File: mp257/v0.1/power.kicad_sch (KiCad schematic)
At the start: 138 parts, among them U26 STPMIC25APQR, U4 STM32MP257FAK3, U9 MCP1501-18xCH

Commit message: Fix ref nums pasted from reference schematic
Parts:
- removed B2: SW_PUSH_SMD_2P, SWI_WE_434121025816, symbol MCD_PARTS_database:U_PMIC_0_SW_PUSH_SMD_2P_MCD_PARTS_database.DbLib
- removed C10, C15, C18, C20, C22 (x2), C23, C26 (x2), C27, C28 (x2), C30, C35 (x2), C36, C8, C9: Capacitor, C0603, symbol MCD_PARTS_database:U_PMIC_1_Capacitor_MCD_PARTS_database.DbLib
- removed C11, C7: Capacitor, C0402, symbol MCD_PARTS_database:U_PMIC_1_Capacitor_MCD_PARTS_database.DbLib
- removed C155, C16, C34, C38: Capacitor, C0402, symbol MCD_PARTS_database:U_PMIC_0_Capacitor_MCD_PARTS_database.DbLib
- removed C17, C37, C39: Capacitor, C0402, symbol MCD_PARTS_database:U_PMIC_2_Capacitor_MCD_PARTS_database.DbLib
- removed C19 (x2), C20, C23, C25, C27, C30, C36: Capacitor, C0805, symbol MCD_PARTS_database:U_PMIC_1_Capacitor_MCD_PARTS_database.DbLib
- removed C50, C51, C71, C82, C85, C96, C97: Capacitor, C0201_MURATA_GRM033_H0P3, symbol MCD_PARTS_database:U_STM32MP25XXAK Power_1_Capacitor_MCD_PARTS_database.DbLib
- removed C50, C51, C52 (x2), C55, C57, C58 (x2), C59 (x2), C60, C61, C62, C64 (x2), C71, C73, C74 (x2), C77, C78, C79, C80, C82, C87, C93, C95: ${ALTIUM_VALUE}, C0201_MURATA_GRM033_H0P3, symbol MCD_PARTS_database:U_STM32MP25XXAK Power_1_Capacitor_MCD_PARTS_database.DbLib
- removed C53, C54, C65, C66, C70 (x2): ${ALTIUM_VALUE}, C0201_MURATA_GRM033_H0P3, symbol MCD_PARTS_database:U_STM32MP25XXAK Power_3_Capacitor_MCD_PARTS_database.DbLib
- removed C87: ~, C0402, symbol MCD_PARTS_database:U_STM32MP25XXAK Power_1_Capacitor_MCD_PARTS_database.DbLib
- removed L5 (x2), L6, L7 (x2): Inductor, IND_2016_MURATA_LQM2MPN2R2NG0, symbol MCD_PARTS_database:U_PMIC_0_Inductor_MCD_PARTS_database.DbLib
- removed L6, L8: Inductor, IND_2520_TOKO_DFE252012P, symbol MCD_PARTS_database:U_PMIC_0_Inductor_MCD_PARTS_database.DbLib
- removed R12, R13, R14, R9: ~, R0402, symbol MCD_PARTS_database:U_PMIC_0_Resistor_MCD_PARTS_database.DbLib
- removed R15: Resistor, R0603, symbol MCD_PARTS_database:U_STM32MP25XXAK Power_0_Resistor_MCD_PARTS_database.DbLib
- removed R17: Resistor, R0402, symbol MCD_PARTS_database:U_STM32MP25XXAK Power_2_Resistor_MCD_PARTS_database.DbLib
- removed U4: STM32MP257FAK3, ICC_TFBGA424_14X14_P050_H1P20_CODE-B0A2, symbol MCD_PARTS_database:U_STM32MP25XXAK Power_0_STM32MP257FAK3_MCD_PARTS_database.Db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
- added C1, C10, C11, C13, C2, C3, C4, C45, C46, C48, C49, C5, C50, C51, C52, C58, C59, C64, C68, C69, C7, C71, C72, C74, C75, C76, C82: ${ALTIUM_VALUE}, C0201_MURATA_GRM033_H0P3, symbol MCD_PARTS_database:U_STM32MP25XXAK Power_1_Capacitor_MCD_PARTS_database.DbLib
- added C12, C44, C47, C6, C70, C8: ${ALTIUM_VALUE}, C0201_MURATA_GRM033_H0P3, symbol MCD_PARTS_database:U_STM32MP25XXAK Power_3_Capacitor_MCD_PARTS_database.DbLib
- added C15, C16, C17, C192, C195, C196, C201: Capacitor, C0201_MURATA_GRM033_H0P3, symbol MCD_PARTS_database:U_STM32MP25XXAK Power_1_Capacitor_MCD_PARTS_database.DbLib
- added C183, C184, C199, C20, C200, C202, C22, C23, C24, C26, C27, C28, C29, C30, C32, C35, C36, C41: Capacitor, C0603, symbol MCD_PARTS_database:U_PMIC_1_Capacitor_MCD_PARTS_database.DbLib
- added C186, C187, C19, C193, C204, C206, C207, C21: Capacitor, C0805, symbol MCD_PARTS_database:U_PMIC_1_Capacitor_MCD_PARTS_database.DbLib
- added C188, C209: Capacitor, C0402, symbol MCD_PARTS_database:U_PMIC_1_Capacitor_MCD_PARTS_database.DbLib
- added C189, C40, C43: Capacitor, C0402, symbol MCD_PARTS_database:U_PMIC_2_Capacitor_MCD_PARTS_database.DbLib
- added C190, C208, C91: Capacitor, C0402, symbol MCD_PARTS_database:U_PMIC_0_Capacitor_MCD_PARTS_database.DbLib
- added C87: ~, C0402, symbol MCD_PARTS_database:U_STM32MP25XXAK Power_1_Capacitor_MCD_PARTS_database.DbLib
- added L1, L3, L5, L6, L7: Inductor, IND_2016_MURATA_LQM2MPN2R2NG0, symbol MCD_PARTS_database:U_PMIC_0_Inductor_MCD_PARTS_database.DbLib
- added L2, L4: Inductor, IND_2520_TOKO_DFE252012P, symbol MCD_PARTS_database:U_PMIC_0_Inductor_MCD_PARTS_database.DbLib
- added R11: Resistor, R0603, symbol MCD_PARTS_database:U_STM32MP25XXAK Power_0_Resistor_MCD_PARTS_database.DbLib
- added R2, R59, R60, R81: ~, R0402, symbol MCD_PARTS_database:U_PMIC_0_Resistor_MCD_PARTS_database.DbLib
- added R269: ~, R0402, symbol MCD_PARTS_database:U_STM32MP25XXAK Power_0_Resistor_MCD_PARTS_database.DbLib
- added R67: Resistor, R0402, symbol MCD_PARTS_database:U_STM32MP25XXAK Power_2_Resistor_MCD_PARTS_database.DbLib
- added U1: STM32MP257FAK3, ICC_TFBGA424_14X14_P050_H1P20_CODE-B0A2, symbol MCD_PARTS_database:U_STM32MP25XXAK Power_0_STM32MP257FAK3_MCD_PARTS_database.Db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
- renumbered C5 to C33
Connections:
- net +3V3: now also C204.2, C206.2, C207.2, C21.2, L7.2
- net +5V: now also C184.2, C188.2, C199.2, C20.2, C209.2, C29.2, C30.2, C32.2
- net 1V8: now also C193.2, L1.2, R269.1, U1.1E1 (VDDA18PLL3), U1.AD22 (VDDA18USB), U1.AE23 (VDDA18COMBOPHY), U1.D18 (VDDIO2), U1.E17 (VDDIO2), U1.F20 (VDDA18DDR), U1.G19 (VDDA18PLL1), U1.G5 (VDDA18LVDS), U1.G7 (VDDA18CSI), U1.G9 (VDDA18DSI), U1.H6 (VDDA18PLL2); no longer C248.2, C250.2
- net GND: now also C1.1, C10.1, C11.1, C12.2, C13.1, C15.1, C16.1, C17.1, C183.1, C184.1, C186.1, C187.1, C188.1, C189.1, C19.1, C190.2, C192.1, C193.1, C195.1, C196.1, C199.1, C2.1, C20.1, C200.1, C201.1, C202.1, C204.1, C206.1, C207.1, C208.2, C209.1, C21.1, C22.1, C23.1, C24.1, C26.1, C27.1, C28.1, C29.1, C3.1, C30.1, C32.1, C35.1, C36.1, C4.1, C40.1, C41.1, C43.1, C44.2, C45.1, C46.1, C47.2, C48.1, C49.1, C5.1, C50.1, C51.1, C52.1, C58.1, C59.1, C6.2, C64.1, C68.1, C69.1, C7.1, C70.2, C71.1, C72.1, C74.1, C75.1, C76.1, C8.2, C82.1, C87.1, C91.2, U1.1A1 (VSS), U1.1A11 (VSS), U1.1A3 (VSS), U1.1A5 (VSS), U1.1A7 (VSS), U1.1A9 (VSS), U1.1B10 (VSS), U1.1B12 (VSS), U1.1B2 (VSS), U1.1B4 (VSS), U1.1B6 (VSS), U1.1B8 (VSS), U1.1E7 (VSS), U1.1E9 (VSS), U1.1F10 (VSS), U1.1F6 (VSS), U1.1F8 (VSS), U1.1G1 (VSS), U1.1G11 (VSS), U1.1G3 (VSS), U1.1G5 (VSS), U1.1H12 (VSS), U1.1H2 (VSS), U1.1H4 (VSS), U1.1J1 (VSS), U1.1J11 (VSS), U1.1J3 (VSS), U1.1J5 (VSS), U1.1J7 (VSS), U1.1J9 (VSS), U1.1K10 (VSS), U1.1K12 (VSS), U1.1K2 (VSS), U1.1K4 (VSS), U1.1K6 (VSS), U1.1K8 (VSS), U1.A1 (VSS), U1.A2 (VSS), U1.A27 (VSS), U1.AC11 (VSS), U1.AC3 (VSSAON), U1.AC5 (VSSA), U1.AF6 (VREFN), U1.AG1 (VSS), U1.AG27 (VSS), U1.C10 (VSS), U1.C6 (VSS), U1.E7 (VSS), U1.F12 (VSS), U1.F14 (VSS), U1.F16 (VSS), U1.F3 (VSS), U1.J7 (VSS), U1.K3 (VSS), U1.V6 (VSS), U1.Y4 (VSS)
- net NRST: now also R81.1
- net NRSTC1MS: now also R59.1
- net PWR_CPU_ON: now also R60.1
- net PWR_ON: now also R2.1
- net VDDA1V8_AON: now also C189.2, U1.AB3 (VDDA18AON)
- net VDDCORE: now also C16.2, C183.2, C192.2, C201.2, C22.2, C23.2, C24.2, C44.1, C45.2, C46.2, C47.1, C48.2, C49.2, C50.2, C51.2, L2.2, R11.1, U1.1C1 (VDDCORE), U1.1C3 (VDDCORE), U1.1C5 (VDDCORE), U1.1D2 (VDDCORE), U1.1D4 (VDDCORE), U1.1E3 (VDDCORE), U1.1E5 (VDDCORE), U1.1F2 (VDDCORE), U1.1F4 (VDDCORE), U1.E5 (VDDCSI), U1.F4 (VDDLVDS), U1.F8 (VDDDSI)
- net VDDCPU: now also C10.2, C11.2, C26.2, C27.2, C28.2, C6.1, C64.2, C68.2, C69.2, C7.2, C8.1, L3.2, U1.1C7 (VDDCPU), U1.1C9 (VDDCPU), U1.1D10 (VDDCPU), U1.1D6 (VDDCPU), U1.1D8 (VDDCPU), U1.F18 (VDDCPU), U1.G15 (VDDCPU), U1.G17 (VDDCPU)
- net VDDGPU: now also C1.2, C2.2, C3.2, C35.2, C36.2, C4.2, C5.2, C52.2, C58.2, C59.2, L4.2, U1.1G7 (VDDGPU), U1.1G9 (VDDGPU), U1.1H10 (VDDGPU), U1.1H6 (VDDGPU), U1.1H8 (VDDGPU), U1.1L7 (VDDGPU), U1.1L9 (VDDGPU), U1.1M10 (VDDGPU), U1.1M6 (VDDGPU), U1.1M8 (VDDGPU)
- net VDDIO: now also C12.1, C17.2, C186.2, C187.2, C19.2, C196.2, C70.1, C71.2, C72.2, C74.2, L6.2, R67.2, U1.1L1 (VDD), U1.1L3 (VDD), U1.1L5 (VDD), U1.1M2 (VDD), U1.1M4 (VDD), U1.D10 (VDDIO3), U1.E11 (VDDIO3), U1.E9 (VDDIO4), U1.G11 (VDDIO4)
- net VDDIO_SDCARD: now also C195.2, U1.D14 (VDDIO1), U1.E13 (VDDIO1)
- net VDD_DDR: now also C13.2, C200.2, C202.2, C41.2, C75.2, C76.2, C82.2, L5.2, U1.1C11 (VDDQDDR), U1.1D12 (VDDQDDR), U1.1E11 (VDDQDDR), U1.1F12 (VDDQDDR), U1.1L11 (VDDQDDR), U1.1M12 (VDDQDDR), U1.M22 (VDDQDDR), U1.N21 (VDDQDDR), U1.R21 (VDDQDDR)
- net VDD_EMMC: now also C190.1
- net VPP_DDR: now also C91.1
- net VREF+: now also C248.2, C250.2, R269.2, U1.AG6 (VREFP)
- net VTT_DDR: now also C40.2
- net at C251.2, R286.2: now also U1.AE21 (VDD33USB), U1.AE22 (VDD33UCPD)
- net at U26.37 (VLX5): now also L1.1
- net at U26.55 (PWRCTRL2): now also R60.2
- net at U26.56 (PWRCTRL1): now also R2.2
- net at C252.2, C260.2: now also C15.2, R11.2, U1.AB20 (VDDCOMBOPHY), U1.AB22 (VDDCOMBOPHYTX), U1.AC21 (VDDPCIECLK)
- net at U26.51 (VLX7): now also L7.1
- net WAKEUP_BUT: now reaches U26.1 (PONKEYn)
- net at U26.19 (VLX4): now also L6.1
- net at U26.23 (VLX3): now also L4.1
- net at U26.26 (VLX2): now also L2.1
- net at U26.31 (RSTn): now also R81.2
- net at U26.40 (VLX1): now also L3.1
- net at U26.45 (REFDDR): now also C43.2
- net at U26.48 (VLX6): now also L5.1
- net at U26.54 (PWRCTRL3): now also R59.2
- net at U26.8 (INTLDO): now also C208.1
- net at C235.2, C244.2, R267.1: now also U1.AB6 (VDDA18ADC)
- net at C225.2: now also U1.R7 (V08CAP)
- new net VBAT: C87.2, R67.1, U1.T6 (VBAT)
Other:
- note removed: "WAKE UP"
- moved on the sheet: C41, C44, U9

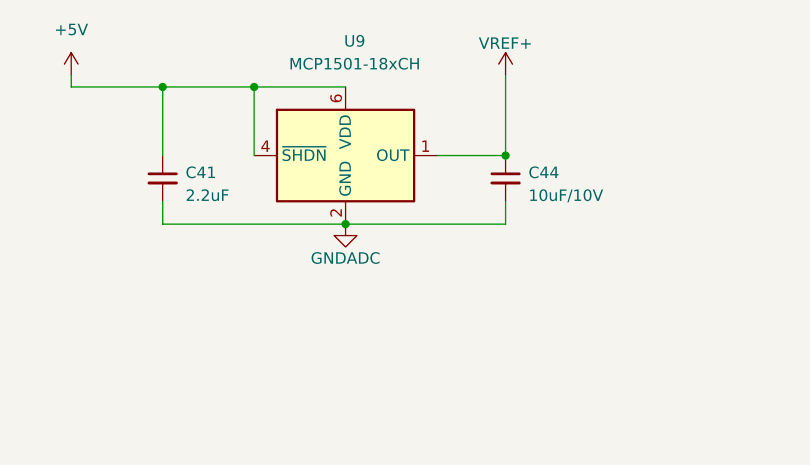
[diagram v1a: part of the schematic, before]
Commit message: Fix all refs: no duplicates
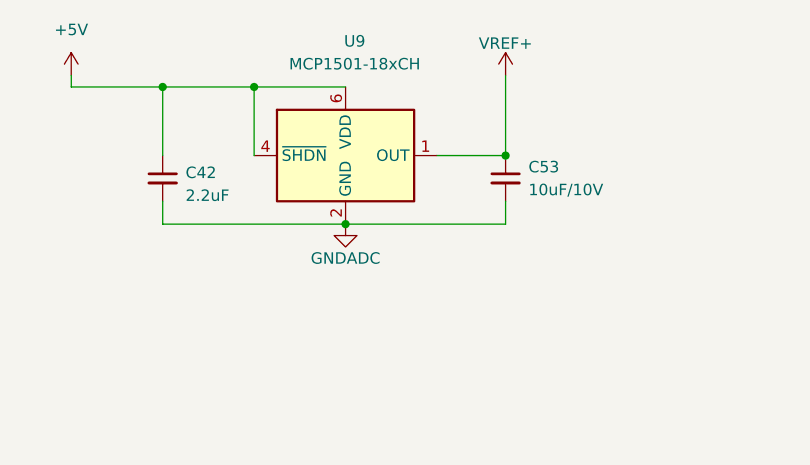
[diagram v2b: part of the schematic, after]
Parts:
- renumbered C41 to C42, C44 to C53

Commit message: WIP: symbols
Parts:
- removed C250: Capacitor, C0201_MURATA_GRM033_H0P3, symbol MCD_PARTS_database:U_STM32MP25XXAK Power_1_Capacitor_MCD_PARTS_database.DbLib
- removed R269: ~, R0402, symbol MCD_PARTS_database:U_STM32MP25XXAK Power_0_Resistor_MCD_PARTS_database.DbLib
- removed R67: Resistor, R0402, symbol MCD_PARTS_database:U_STM32MP25XXAK Power_2_Resistor_MCD_PARTS_database.DbLib
- added NT1: NetTie, 4ms_SolderJumper:NetTie-2_SMD_Pad0.16mm_6mil, symbol 4ms_Net_Tie:NetTie
- U1: symbol MCD_PARTS_database:U_STM32MP25XXAK Power_0_STM32MP257FAK3_MCD_PARTS_database.DbLib -> 4ms_IC:STM32MP257FAKx
- U26: footprint ICC_QFN56-EPAD_6P5X6P5_P040 -> 4ms_Package_QFP:QFN-56_EP_7x7_Pitch0.4mm; symbol MCD_PARTS_database:U_PMIC_0_STPMIC2_MCD_PARTS_database.DbLib -> 4ms_IC:STPMIC25APQR; ALTIUM_VALUE STPMIC25APQR -> (none); COMPONENTLINK1DESCRIPTION Datasheet -> (none); COMPONENTLINK1URL http://tunmcdsvn.tun.st.com/Component_Documentation_Library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 -> (none); COMPONENT_COUNTRY_OF_ORIGIN Unknown -> (none); ID 5116 -> (none); INTERNAL_PART_NUMBER MCD-03000 -> (none); MANUFACTURER STMICROELECTRONICS -> (none); MANUFACTURER_PART_NUMBER STPMIC25APQR -> (none); Manufacturer (none) -> STMICROELECTRONICS; ORDER_CODE_DIGIKEY N/A -> (none); ORDER_CODE_FARNELL N/A -> (none); ORDER_CODE_RS N/A -> (none); PACKAGE VQFN -> (none); PART_PREFERENCE Recommended -> (none); PART_TYPE IC -> (none); Part Number (none) -> STPMIC25APQR; SHOWFIELDS YES -> (none); STATUS Released -> (none)
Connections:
- net VDDIO is gone; now on net VDD_IO: C12.1, C17.2, C186.2, C187.2, C19.2, C196.2, C70.1, C71.2, C72.2, C74.2, L6.2, LNK11.2, R260.2, R261.2, U1.1L1 (VDD), U1.1L3 (VDD), U1.1L5 (VDD), U1.1M2 (VDD), U1.1M4 (VDD), U1.D10 (VDDIO3), U1.E11 (VDDIO3), U1.E9 (VDDIO4), U1.G11 (VDDIO4), U26.29 (VIO)
- net GND: now also NT1.1; no longer U1.AF6 (VREFN)
- net GNDADC: now also U1.AF6 (VREFN), NT1.2
- net 1V8 renamed +1V8
- net 5V_VCONN: no longer names the net of C1141.1, U26.5 (LDO6OUT)
- net VBAT renamed VDD_IO
- net VDD3V3_USB renamed VDD_USB
- net VDDA1V8_AON renamed VDDA_1V8
- net VDDCORE renamed VDD_CORE
- net VDDCPU renamed VDD_CPU
- net VDDGPU renamed VDD_GPU
- net VDD_EMMC: no longer names the net of C190.1, U26.16 (LDO2OUT)
- net VDD_SDCARD: no longer names the net of C142.1, U26.4 (LDO7OUT)
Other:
- note added: "5V_VCONN"
- note added: "Not used"
- note added: "VDD_EMMC"
- note added: "VDD_SDCARD"
- moved on the sheet: C1141, C142, C16, C217, C91

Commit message: Updated RAM and STM32MP2 footprints to 4ms lib
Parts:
- U1: footprint ICC_TFBGA424_14X14_P050_H1P20_CODE-B0A2 -> 4ms_Package_QFP:TFBGA-424_14x14mm_P0.5_STM_AK

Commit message: Updating parts to 4ms lib
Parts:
- C1, C10, C11, C13, C2, C3, C4, C45, C46, C48, C49, C5, C50, C51, C52, C58, C59, C64, C68, C69, C7, C71, C72, C74, C75, C76, C82: value ${ALTIUM_VALUE} -> 1uF_0201_4V; footprint C0201_MURATA_GRM033_H0P3 -> 4ms_Capacitor:C_0201; symbol MCD_PARTS_database:U_STM32MP25XXAK Power_1_Capacitor_MCD_PARTS_database.DbLib -> 4ms_Capacitor:1uF_0201_4V; ALTIUM_VALUE 1uF -> (none); COMPONENTLINK1URL http://tunmcdsvn.tun.st.com/Component_Documentation_Library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 -> (none); COMPONENT_COUNTRY_OF_ORIGIN Japan -> (none); Display (none) -> 1uF; ID 4483 -> (none); INTERNAL_PART_NUMBER MCD-02377 -> (none); JLCPCB ID (none) -> C272877; MANUFACTURER MURATA -> (none); MANUFACTURER_PART_NUMBER GRM033R60J105MEA2 -> (none); Manufacturer (none) -> Yageo; Manufacturer 2 (none) -> Murata; ORDER_CODE_DIGIKEY 490-7229-2-ND -> (none); ORDER_CODE_FARNELL 2470448 -> (none); ORDER_CODE_RS 820-0643 -> (none); PACKAGE 0201 -> (none); PART_PREFERENCE Recommended -> (none); PART_TYPE Capacitor -> (none); Part Number (none) -> CC0201MRX5R5BB105; Part Number 2 (none) -> GRM033D70G105ME01D; Production Stage (none) -> A; SHOWFIELDS YES -> (none); STATUS Checked -> (none); Specifications (none) -> 1uF, Min. 4V 10%, X7R or X5R or X6S or similar
- C1141, C142, C190, C208, C217, C91: value Capacitor -> 4.7uF_0402_6.3V; footprint C0402 -> 4ms_Capacitor:C_0402; symbol MCD_PARTS_database:U_PMIC_0_Capacitor_MCD_PARTS_database.DbLib -> 4ms_Capacitor:4.7uF_0402_6.3V; ALTIUM_VALUE 4.7uF -> (none); COMPONENTLINK1URL http://tunmcdsvn.tun.st.com/Component_Documentation_Library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 -> (none); COMPONENT_COUNTRY_OF_ORIGIN Japan -> (none); Display (none) -> 4.7uF; ID 3456 -> (none); INTERNAL_PART_NUMBER MCD-01356 -> (none); JLCPCB ID (none) -> C23733; MANUFACTURER MURATA -> (none); MANUFACTURER_PART_NUMBER GRM155R60J475ME47 -> (none); Manufacturer (none) -> Murata; ORDER_CODE_DIGIKEY 490-5915-1-ND -> (none); ORDER_CODE_FARNELL 2666407 -> (none); ORDER_CODE_RS 814-5230 -> (none); PACKAGE 0402 -> (none); PART_PREFERENCE Recommended -> (none); PART_TYPE Capacitor -> (none); Part Number (none) -> GRM155R60J475ME47; Production Stage (none) -> A; SHOWFIELDS YES -> (none); STATUS Released -> (none); Specifications (none) -> 4.7uF, Min. 6.3V 20%, X7R or X5R or similar
- C12, C44, C47, C6, C70, C77, C8: value ${ALTIUM_VALUE} -> 1uF_0201_4V; footprint C0201_MURATA_GRM033_H0P3 -> 4ms_Capacitor:C_0201; symbol MCD_PARTS_database:U_STM32MP25XXAK Power_3_Capacitor_MCD_PARTS_database.DbLib -> 4ms_Capacitor:1uF_0201_4V; ALTIUM_VALUE 1uF -> (none); COMPONENTLINK1URL http://tunmcdsvn.tun.st.com/Component_Documentation_Library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 -> (none); COMPONENT_COUNTRY_OF_ORIGIN Japan -> (none); Display (none) -> 1uF; ID 4483 -> (none); INTERNAL_PART_NUMBER MCD-02377 -> (none); JLCPCB ID (none) -> C272877; MANUFACTURER MURATA -> (none); MANUFACTURER_PART_NUMBER GRM033R60J105MEA2 -> (none); Manufacturer (none) -> Yageo; Manufacturer 2 (none) -> Murata; ORDER_CODE_DIGIKEY 490-7229-2-ND -> (none); ORDER_CODE_FARNELL 2470448 -> (none); ORDER_CODE_RS 820-0643 -> (none); PACKAGE 0201 -> (none); PART_PREFERENCE Recommended -> (none); PART_TYPE Capacitor -> (none); Part Number (none) -> CC0201MRX5R5BB105; Part Number 2 (none) -> GRM033D70G105ME01D; Production Stage (none) -> A; SHOWFIELDS YES -> (none); STATUS Checked -> (none); Specifications (none) -> 1uF, Min. 4V 10%, X7R or X5R or X6S or similar
- C15, C252, C260: value Capacitor -> 1uF_0201_4V; footprint C0201_MURATA_GRM033_H0P3 -> 4ms_Capacitor:C_0201; symbol MCD_PARTS_database:U_STM32MP25XXAK Power_1_Capacitor_MCD_PARTS_database.DbLib -> 4ms_Capacitor:1uF_0201_4V; ALTERNATE_MANUFACTURER N/A -> (none); ALTERNATE_MANUFACTURER_PART_NUMBER N/A -> (none); ALTIUM_VALUE 1uF -> (none); COMPONENTLINK1URL http://tunmcdsvn.tun.st.com/Component_Documentation_Library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 -> (none); COMPONENT_COUNTRY_OF_ORIGIN Japan -> (none); Display (none) -> 1uF; ID 4483 -> (none); INTERNAL_PART_NUMBER MCD-02377 -> (none); JLCPCB ID (none) -> C272877; MANUFACTURER MURATA -> (none); MANUFACTURER_PART_NUMBER GRM033R60J105MEA2 -> (none); Manufacturer (none) -> Yageo; Manufacturer 2 (none) -> Murata; ORDER_CODE_DIGIKEY 490-7229-2-ND -> (none); ORDER_CODE_FARNELL 2470448 -> (none); ORDER_CODE_RS 820-0643 -> (none); PACKAGE 0201 -> (none); PART_PREFERENCE Recommended -> (none); PART_TYPE Capacitor -> (none); Part Number (none) -> CC0201MRX5R5BB105; Part Number 2 (none) -> GRM033D70G105ME01D; Production Stage (none) -> A; SHOWFIELDS YES -> (none); STATUS Checked -> (none); Specifications (none) -> 1uF, Min. 4V 10%, X7R or X5R or X6S or similar
- C152, C157, C186, C187, C19, C193, C204, C206, C207, C21: value Capacitor -> 22uF_0805_10V; footprint C0805 -> 4ms_Capacitor:C_0805; symbol MCD_PARTS_database:U_PMIC_1_Capacitor_MCD_PARTS_database.DbLib -> 4ms_Capacitor:22uF_0805_10V; ALTIUM_VALUE 22uF -> (none); COMPONENTLINK1URL http://tunmcdsvn.tun.st.com/Component_Documentation_Library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 -> (none); COMPONENT_COUNTRY_OF_ORIGIN China, Japan -> (none); Display (none) -> 22uF/10V; ID 5255 -> (none); INTERNAL_PART_NUMBER MCD-03139 -> (none); JLCPCB ID (none) -> C45783; MANUFACTURER MURATA -> (none); MANUFACTURER_PART_NUMBER GRM21BR61A226ME51L -> (none); Manufacturer (none) -> Taiyo Yuden; ORDER_CODE_DIGIKEY 490-10511-2-ND -> (none); ORDER_CODE_FARNELL 2494270 -> (none); ORDER_CODE_RS N/A -> (none); PACKAGE 0805 -> (none); PART_PREFERENCE Recommended -> (none); PART_TYPE Capacitor -> (none); Part Number (none) -> LMK212BBJ226MG-T; Production Stage (none) -> A; SHOWFIELDS YES -> (none); STATUS Checked -> (none); Specifications (none) -> 22uF, Min. 10V, 20%, X5R or X7S or similar, 0805, MLCC
- C153, C154, C188: value Capacitor -> 1uF_0402_25V; footprint C0402 -> 4ms_Capacitor:C_0402; symbol MCD_PARTS_database:U_PMIC_1_Capacitor_MCD_PARTS_database.DbLib -> 4ms_Capacitor:1uF_0402_25V; ALTIUM_VALUE 1uF -> (none); COMPONENTLINK1URL http://tunmcdsvn.tun.st.com/Component_Documentation_Library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 -> (none); COMPONENT_COUNTRY_OF_ORIGIN Japan -> (none); Display (none) -> 1uF; ID 2772 -> (none); INTERNAL_PART_NUMBER MCD-00095 -> (none); JLCPCB ID (none) -> C52923; MANUFACTURER MURATA -> (none); MANUFACTURER_PART_NUMBER GRM155R61E105KA12 -> (none); Manufacturer (none) -> Taiyo Yuden; Manufacturer 2 (none) -> Murata; ORDER_CODE_DIGIKEY 490-10017-1-ND -> (none); ORDER_CODE_FARNELL 2218855 -> (none); ORDER_CODE_RS 846-7287 -> (none); PACKAGE 0402 -> (none); PART_PREFERENCE Recommended -> (none); PART_TYPE Capacitor -> (none); Part Number (none) -> GMK105CC6105KV-F; Part Number 2 (none) -> GRM155C81E105ME11J; Production Stage (none) -> A; SHOWFIELDS YES -> (none); STATUS Released -> (none); Specifications (none) -> 1uF, Min. 25V, 0402, Ceramic/MLCC
- C156, C189: value Capacitor -> 4.7uF_0402_6.3V; footprint C0402 -> 4ms_Capacitor:C_0402; symbol MCD_PARTS_database:U_PMIC_2_Capacitor_MCD_PARTS_database.DbLib -> 4ms_Capacitor:4.7uF_0402_6.3V; ALTIUM_VALUE 4.7uF -> (none); COMPONENTLINK1URL http://tunmcdsvn.tun.st.com/Component_Documentation_Library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 -> (none); COMPONENT_COUNTRY_OF_ORIGIN Japan -> (none); Display (none) -> 4.7uF; ID 3456 -> (none); INTERNAL_PART_NUMBER MCD-01356 -> (none); JLCPCB ID (none) -> C23733; MANUFACTURER MURATA -> (none); MANUFACTURER_PART_NUMBER GRM155R60J475ME47 -> (none); Manufacturer (none) -> Murata; ORDER_CODE_DIGIKEY 490-5915-1-ND -> (none); ORDER_CODE_FARNELL 2666407 -> (none); ORDER_CODE_RS 814-5230 -> (none); PACKAGE 0402 -> (none); PART_PREFERENCE Recommended -> (none); PART_TYPE Capacitor -> (none); Part Number (none) -> GRM155R60J475ME47; Production Stage (none) -> A; SHOWFIELDS YES -> (none); STATUS Released -> (none); Specifications (none) -> 4.7uF, Min. 6.3V 20%, X7R or X5R or similar
- C16, C17, C192, C195, C196, C201, C220, C234, C236, C237, C238, C239, C240, C244, C246, C248, C251, C253: value Capacitor -> 100nF_0201_16V; footprint C0201_MURATA_GRM033_H0P3 -> 4ms_Capacitor:C_0201; symbol MCD_PARTS_database:U_STM32MP25XXAK Power_1_Capacitor_MCD_PARTS_database.DbLib -> 4ms_Capacitor:100nF_0201_16V; ALTERNATE_MANUFACTURER N/A -> (none); ALTERNATE_MANUFACTURER_PART_NUMBER N/A -> (none); ALTIUM_VALUE 100nF -> (none); COMPONENTLINK1URL http://tunmcdsvn.tun.st.com/Component_Documentation_Library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 -> (none); COMPONENT_COUNTRY_OF_ORIGIN Japan -> (none); Display (none) -> 0.1uF; ID 3635 -> (none); INTERNAL_PART_NUMBER MCD-01535 -> (none); JLCPCB ID (none) -> C711071; MANUFACTURER MURATA -> (none); MANUFACTURER_PART_NUMBER GRM033R61A104KE15 -> (none); Manufacturer (none) -> Murata; Manufacturer 2 (none) -> Yageo; ORDER_CODE_DIGIKEY 490-5881-1-ND -> (none); ORDER_CODE_FARNELL 2470450 -> (none); ORDER_CODE_RS 790-2742 -> (none); PACKAGE 0201 -> (none); PART_PREFERENCE Recommended -> (none); PART_TYPE Capacitor -> (none); Part Number (none) -> GRT033C81E104KE01D; Part Number 2 (none) -> CC0201MRX5R6BB104; Production Stage (none) -> A; SHOWFIELDS YES -> (none); STATUS Checked -> (none); Specifications (none) -> 0.1uF, Min. 16V 10%, X7R or X5R or X6S or similar
- C183, C200, C202, C22, C23, C24, C26, C27, C28, C34, C35, C36, C37, C41: value Capacitor -> 22uF_0603_6.3V; footprint C0603 -> 4ms_Capacitor:C_0603; symbol MCD_PARTS_database:U_PMIC_1_Capacitor_MCD_PARTS_database.DbLib -> 4ms_Capacitor:22uF_0603_6.3V; ALTERNATE_MANUFACTURER N/A -> (none); ALTERNATE_MANUFACTURER_PART_NUMBER N/A -> (none); ALTIUM_VALUE 22uF -> (none); COMPONENTLINK1DESCRIPTION Part_Information -> (none); COMPONENTLINK1URL http://tunmcdsvn.tun.st.com/Component_Documentation_Library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 -> (none); COMPONENT_COUNTRY_OF_ORIGIN Japan -> (none); Display (none) -> 22uF/6.3V; ID 2766 -> (none); INTERNAL_PART_NUMBER MCD-00100 -> (none); JLCPCB ID (none) -> C59461; MANUFACTURER MURATA -> (none); MANUFACTURER_PART_NUMBER GRM188R60J226MEA0J -> (none); Manufacturer (none) -> Murata; ORDER_CODE_DIGIKEY 490-7612-2-ND -> (none); ORDER_CODE_FARNELL N/A -> (none); ORDER_CODE_RS N/A -> (none); PACKAGE 0603 -> (none); PART_PREFERENCE Recommended -> (none); PART_TYPE Capacitor -> (none); Part Number (none) -> GRM188R60J226MEA0J; Production Stage (none) -> A; SHOWFIELDS YES -> (none); STATUS Released -> (none); Specifications (none) -> 22uF, 6.3V,10%,X5R or X7R,0603
- C184, C199, C20, C29, C30, C32, C38: value Capacitor -> 10uF_0603_10V; footprint C0603 -> 4ms_Capacitor:C_0603; symbol MCD_PARTS_database:U_PMIC_1_Capacitor_MCD_PARTS_database.DbLib -> 4ms_Capacitor:10uF_0603_10V; ALTERNATE_MANUFACTURER N/A -> (none); ALTERNATE_MANUFACTURER_PART_NUMBER N/A -> (none); ALTIUM_VALUE 10uF -> (none); COMPONENTLINK1DESCRIPTION Part_Information -> (none); COMPONENTLINK1URL http://tunmcdsvn.tun.st.com/Component_Documentation_Library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 -> (none); COMPONENT_COUNTRY_OF_ORIGIN Japan -> (none); Display (none) -> 10uF/10V; ID 2770 -> (none); INTERNAL_PART_NUMBER MCD-00099 -> (none); JLCPCB ID (none) -> C19702; MANUFACTURER MURATA -> (none); MANUFACTURER_PART_NUMBER GRM188R61A106KE69D -> (none); Manufacturer (none) -> Murata; ORDER_CODE_DIGIKEY 490-10474-1-ND -> (none); ORDER_CODE_FARNELL 2494233 -> (none); ORDER_CODE_RS 170-6168 -> (none); PACKAGE 0603 -> (none); PART_PREFERENCE Recommended -> (none); PART_TYPE Capacitor -> (none); Part Number (none) -> GRM188R61A106KE69D; Production Stage (none) -> A; SHOWFIELDS YES -> (none); STATUS Released -> (none); Specifications (none) -> 10uF, Min. 10V X5R 10%
- C209: value Capacitor -> 4.7uF_0402_6.3V; footprint C0402 -> 4ms_Capacitor:C_0402; symbol MCD_PARTS_database:U_PMIC_1_Capacitor_MCD_PARTS_database.DbLib -> 4ms_Capacitor:4.7uF_0402_6.3V; ALTIUM_VALUE 4.7uF -> (none); COMPONENTLINK1URL http://tunmcdsvn.tun.st.com/Component_Documentation_Library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 -> (none); COMPONENT_COUNTRY_OF_ORIGIN Japan -> (none); Display (none) -> 4.7uF; ID 3456 -> (none); INTERNAL_PART_NUMBER MCD-01356 -> (none); JLCPCB ID (none) -> C23733; MANUFACTURER MURATA -> (none); MANUFACTURER_PART_NUMBER GRM155R60J475ME47 -> (none); Manufacturer (none) -> Murata; ORDER_CODE_DIGIKEY 490-5915-1-ND -> (none); ORDER_CODE_FARNELL 2666407 -> (none); ORDER_CODE_RS 814-5230 -> (none); PACKAGE 0402 -> (none); PART_PREFERENCE Recommended -> (none); PART_TYPE Capacitor -> (none); Part Number (none) -> GRM155R60J475ME47; Production Stage (none) -> A; SHOWFIELDS YES -> (none); STATUS Released -> (none); Specifications (none) -> 4.7uF, Min. 6.3V 20%, X7R or X5R or similar
- C225: value Capacitor -> 4.7uF_0201_6.3V; footprint C0201_H0P5 -> 4ms_Capacitor:C_0201; symbol MCD_PARTS_database:U_STM32MP25XXAK Power_1_Capacitor_MCD_PARTS_database.DbLib -> 4ms_Capacitor:4.7uF_0201_6.3V; ALTERNATE_MANUFACTURER N/A -> (none); ALTERNATE_MANUFACTURER_PART_NUMBER N/A -> (none); ALTIUM_VALUE 4.7uF -> (none); COMPONENTLINK1URL http://tunmcdsvn.tun.st.com/Component_Documentation_Library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 -> (none); COMPONENT_COUNTRY_OF_ORIGIN Japan -> (none); Display (none) -> 4.7uF; ID 3634 -> (none); INTERNAL_PART_NUMBER MCD-01534 -> (none); MANUFACTURER MURATA -> (none); MANUFACTURER_PART_NUMBER GRM035R60J475ME15 -> (none); ORDER_CODE_DIGIKEY 490-13230-1-ND -> (none); ORDER_CODE_FARNELL N/A -> (none); ORDER_CODE_RS N/A -> (none); PACKAGE 0201 -> (none); PART_PREFERENCE Recommended -> (none); PART_TYPE Capacitor -> (none); Production Stage (none) -> A; SHOWFIELDS YES -> (none); STATUS Checked -> (none); Specifications (none) -> 4.7uF, Min. 6.3V 10%, X7R or X5R or X6S or similar
- C235: value Capacitor -> 2.2uF_0201_10V; footprint C0201_H0P5 -> 4ms_Capacitor:C_0201; symbol MCD_PARTS_database:U_STM32MP25XXAK Power_1_Capacitor_MCD_PARTS_database.DbLib -> 4ms_Capacitor:2.2uF_0201_10V; ALTIUM_VALUE 2.2uF -> (none); COMPONENTLINK1URL http://tunmcdsvn.tun.st.com/Component_Documentation_Library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 -> (none); COMPONENT_COUNTRY_OF_ORIGIN Japan -> (none); Display (none) -> 2.2uF; ID 4335 -> (none); INTERNAL_PART_NUMBER MCD-02235 -> (none); MANUFACTURER MURATA -> (none); MANUFACTURER_PART_NUMBER GRM033R61A225KE47D -> (none); ORDER_CODE_DIGIKEY 490-13227-1-ND -> (none); ORDER_CODE_FARNELL NA -> (none); ORDER_CODE_RS NA -> (none); PACKAGE 0201 -> (none); PART_PREFERENCE Recommended -> (none); PART_TYPE Capacitor -> (none); Production Stage (none) -> A; SHOWFIELDS YES -> (none); STATUS Checked -> (none); Specifications (none) -> 2.2uF, Min. 10V 10%, X7R or X5R or X6S or similar
- C33: value Capacitor -> 10nF_0402_16V; footprint C0402 -> 4ms_Capacitor:C_0402; symbol MCD_PARTS_database:U_STM32MP25XXAK I_Os_2_Capacitor_MCD_PARTS_database.DbLib -> 4ms_Capacitor:10nF_0402_16V; ALTIUM_VALUE 10nF -> (none); COMPONENTLINK1DESCRIPTION Datasheet -> (none); COMPONENTLINK1URL http://tunmcdsvn.tun.st.com/Component_Datasheet_Library/Tru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 -> (none); Display (none) -> 10nF; ECCN_EU n/a -> (none); ECCN_US n/a -> (none); INITIAL_BOARD_REFERENCE MB1274 -> (none); INTERNAL_PART_NUMBER MCD-00011 -> (none); JLCPCB ID (none) -> C15195; MANUFACTURER YAGEO -> (none); MANUFACTURER_PART_NUMBER CC0402KRX7R7BB103 -> (none); Manufacturer (none) -> Yageo; PACKAGE C0402 -> (none); PART_TYPE Capacitor -> (none); PROVIDED_BY SUBCO -> (none); Part Number (none) -> CC0402KRX7R7BB103; Production Stage (none) -> A; STATUS Released -> (none); Specifications (none) -> 10nF, Min. 16V 10%, X7R or X5R or similar
- C39: value Capacitor -> 10uF_0402_6.3V; footprint C__VIRGIL_AAA__JOB_ALTIUM_STM_Library_Altium_Library_Altium_STM-LMS_MCD_PARTS.PcbLib:C0402 -> 4ms_Capacitor:C_0402; symbol MCD_PARTS_database:U_PMIC_1_Capacitor_MCD_PARTS_database.DbLib -> 4ms_Capacitor:10uF_0402_6.3V; ALTIUM_VALUE 10uF -> (none); COMPONENTLINK1URL http://tunmcdsvn.tun.st.com/Component_Documentation_Library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 -> (none); Display (none) -> 10uF; ID 5256 -> (none); INTERNAL_PART_NUMBER MCD-03140 -> (none); MANUFACTURER MURATA -> (none); MANUFACTURER_PART_NUMBER GRM155R60J106ME05D -> (none); ORDER_CODE_DIGIKEY 490-GRM155R60J106ME05DTR-ND -> (none); ORDER_CODE_FARNELL 3784428 -> (none); ORDER_CODE_RS N/A -> (none); PACKAGE 0402 -> (none); PART_PREFERENCE Recommended -> (none); PART_TYPE Capacitor -> (none); Production Stage (none) -> A; SHOWFIELDS YES -> (none); STATUS New -> (none); Specifications (none) -> 10uF, Min. 6.3V, 0402, Ceramic/MLCC
- C40: value Capacitor -> 10uF_0402_6.3V; footprint C0402 -> 4ms_Capacitor:C_0402; symbol MCD_PARTS_database:U_PMIC_2_Capacitor_MCD_PARTS_database.DbLib -> 4ms_Capacitor:10uF_0402_6.3V; ALTIUM_VALUE 10uF -> (none); COMPONENTLINK1URL http://tunmcdsvn.tun.st.com/Component_Documentation_Library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 -> (none); COMPONENT_COUNTRY_OF_ORIGIN China, Japan -> (none); Display (none) -> 10uF; ID 5256 -> (none); INTERNAL_PART_NUMBER MCD-03140 -> (none); MANUFACTURER MURATA -> (none); MANUFACTURER_PART_NUMBER GRM155R60J106ME05D -> (none); ORDER_CODE_DIGIKEY 490-GRM155R60J106ME05DTR-ND -> (none); ORDER_CODE_FARNELL 3784428 -> (none); ORDER_CODE_RS N/A -> (none); PACKAGE 0402 -> (none); PART_PREFERENCE Recommended -> (none); PART_TYPE Capacitor -> (none); Production Stage (none) -> A; SHOWFIELDS YES -> (none); STATUS Checked -> (none); Specifications (none) -> 10uF, Min. 6.3V, 0402, Ceramic/MLCC
- C43: value Capacitor -> 1uF_0402_25V; footprint C0402 -> 4ms_Capacitor:C_0402; symbol MCD_PARTS_database:U_PMIC_2_Capacitor_MCD_PARTS_database.DbLib -> 4ms_Capacitor:1uF_0402_25V; ALTIUM_VALUE 1uF -> (none); COMPONENTLINK1URL http://tunmcdsvn.tun.st.com/Component_Documentation_Library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 -> (none); COMPONENT_COUNTRY_OF_ORIGIN Japan -> (none); Display (none) -> 1uF; ID 2772 -> (none); INTERNAL_PART_NUMBER MCD-00095 -> (none); JLCPCB ID (none) -> C52923; MANUFACTURER MURATA -> (none); MANUFACTURER_PART_NUMBER GRM155R61E105KA12 -> (none); Manufacturer (none) -> Taiyo Yuden; Manufacturer 2 (none) -> Murata; ORDER_CODE_DIGIKEY 490-10017-1-ND -> (none); ORDER_CODE_FARNELL 2218855 -> (none); ORDER_CODE_RS 846-7287 -> (none); PACKAGE 0402 -> (none); PART_PREFERENCE Recommended -> (none); PART_TYPE Capacitor -> (none); Part Number (none) -> GMK105CC6105KV-F; Part Number 2 (none) -> GRM155C81E105ME11J; Production Stage (none) -> A; SHOWFIELDS YES -> (none); STATUS Released -> (none); Specifications (none) -> 1uF, Min. 25V, 0402, Ceramic/MLCC
- C87: value ~ -> 100nF_0402_16V; footprint C0402 -> 4ms_Capacitor:C_0402; symbol MCD_PARTS_database:U_STM32MP25XXAK Power_1_Capacitor_MCD_PARTS_database.DbLib -> 4ms_Capacitor:100nF_0402_16V; ALTERNATE_EMS M -> (none); ALTERNATE_MANUFACTURER MURATA -> (none); ALTERNATE_MANUFACTURER_PART_NUMBER GCM155R71C104KA55D -> (none); ALTIUM_VALUE 100nF -> (none); COMPONENTLINK1DESCRIPTION Datasheet -> (none); COMPONENTLINK1URL http://tunmcdsvn.tun.st.com/Component_Documentation_Library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 -> (none); COMPONENT_COUNTRY_OF_ORIGIN China -> (none); Display (none) -> 0.1uF; ECCN_EU n/a -> (none); ECCN_US n/a -> (none); ID 2474 -> (none); INITIAL_BOARD_REFERENCE MB1274 -> (none); INTERNAL_PART_NUMBER MCD-00006 -> (none); JLCPCB ID (none) -> C1525; MANUFACTURER YAGEO -> (none); MANUFACTURER_PART_NUMBER CC0402KRX7R7BB104 -> (none); Manufacturer (none) -> Murata; Manufacturer 2 (none) -> Yageo; ORDER_CODE_DIGIKEY 311-1338-1-ND -> (none); ORDER_CODE_FARNELL 9402047 -> (none); ORDER_CODE_RS 616-9701 -> (none); PACKAGE 0402 -> (none); PARTIAL_ALTERNATE_INTERNAL_PART_NUMBER MCD-03299 -> (none); PART_PREFERENCE Recommended -> (none); PART_TYPE Capacitor -> (none); PROVIDED_BY SUBCO -> (none); Part Number (none) -> GCM155R71C104KA55D; Part Number 2 (none) -> CC0402KRX7R7BB104; Production Stage (none) -> A; SHOWFIELDS YES -> (none); STATUS Released -> (none); Specifications (none) -> 0.1uF, Min. 16V 10%, X7R or X5R or similar
- R11: value Resistor -> 0Ω_0603; footprint R0603 -> 4ms_Resistor:R_0603; symbol MCD_PARTS_database:U_STM32MP25XXAK Power_0_Resistor_MCD_PARTS_database.DbLib -> 4ms_Resistor_0603:0Ω_0603; ALTIUM_VALUE 0R -> (none); COMPONENTLINK1URL http://tunmcdsvn.tun.st.com/Component_Documentation_Library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 -> (none); COMPONENT_COUNTRY_OF_ORIGIN China -> (none); Display (none) -> 0Ω; ID 2536 -> (none); INTERNAL_PART_NUMBER MCD-00056 -> (none); JLCPCB ID (none) -> C21189; MANUFACTURER YAGEO -> (none); MANUFACTURER_PART_NUMBER RC0603JR-070RL -> (none); Manufacturer (none) -> Yageo; ORDER_CODE_DIGIKEY 311-0.0GRCT-ND -> (none); ORDER_CODE_FARNELL 9233130RL -> (none); ORDER_CODE_RS N/A -> (none); PACKAGE 0603 -> (none); PART_PREFERENCE Recommended -> (none); PART_TYPE Resistor -> (none); Part Number (none) -> RC0603FR-070RL; Production Stage (none) -> A; SHOWFIELDS YES -> (none); STATUS Released -> (none); Specifications (none) -> 0Ω, 1%, 1/10W, 0603
- R2, R46, R59, R60, R81: value ~ -> 0Ω_0402; footprint R0402 -> 4ms_Resistor:R_0402; symbol MCD_PARTS_database:U_PMIC_0_Resistor_MCD_PARTS_database.DbLib -> 4ms_Resistor_0402:0Ω_0402; ALTERNATE_MANUFACTURER N/A -> (none); ALTERNATE_MANUFACTURER_PART_NUMBER N/A -> (none); ALTIUM_VALUE 0R -> (none); COMPONENTLINK1DESCRIPTION Datasheet -> (none); COMPONENTLINK1URL http://tunmcdsvn.tun.st.com/Component_Documentation_Library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 -> (none); COMPONENT_COUNTRY_OF_ORIGIN China -> (none); Display (none) -> 0Ω; ECCN_EU NEC -> (none); ECCN_US EAR99 -> (none); ID 2540 -> (none); INITIAL_BOARD_REFERENCE mb1274 -> (none); INTERNAL_PART_NUMBER MCD-00052 -> (none); JLCPCB ID (none) -> C106231; MANUFACTURER YAGEO -> (none); MANUFACTURER_PART_NUMBER RC0402JR-070RL -> (none); Manufacturer (none) -> Yageo; ORDER_CODE_DIGIKEY 311-0.0JRCT-ND -> (none); ORDER_CODE_FARNELL 9232516RL -> (none); ORDER_CODE_RS 618-5804 -> (none); PACKAGE 0402 -> (none); PART_PREFERENCE Recommended -> (none); PART_TYPE Resistor -> (none); PROVIDED_BY SUBCO -> (none); Part Number (none) -> RC0402FR-070RL; Production Stage (none) -> A; SHOWFIELDS YES -> (none); STATUS Released -> (none); Specifications (none) -> 0Ω, 1%, 1/16W, 0402
- R260, R261: value Resistor -> 1.5k_0402; footprint R0402 -> 4ms_Resistor:R_0402; symbol MCD_PARTS_database:U_STM32MP25XXAK I_Os_0_Resistor_MCD_PARTS_database.DbLib -> 4ms_Resistor_0402:1.5k_0402; ALTIUM_VALUE 1K5 -> (none); COMPONENTLINK1DESCRIPTION Datasheet -> (none); COMPONENTLINK1URL http://tunmcdsvn.tun.st.com/Component_Documentation_Library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 -> (none); COMPONENT_COUNTRY_OF_ORIGIN China -> (none); Display (none) -> 1.5k; ID 2524 -> (none); INTERNAL_PART_NUMBER MCD-00068 -> (none); JLCPCB ID (none) -> C114759; MANUFACTURER YAGEO -> (none); MANUFACTURER_PART_NUMBER RC0402FR-071K5L -> (none); Manufacturer (none) -> Yageo; ORDER_CODE_DIGIKEY 311-1.50KLRCT-ND -> (none); ORDER_CODE_FARNELL 9239251 -> (none); ORDER_CODE_RS N/A -> (none); PACKAGE 0402 -> (none); PART_PREFERENCE Recommended -> (none); PART_TYPE Resistor -> (none); Part Number (none) -> RC0402FR-071K5L; Production Stage (none) -> A; SHOWFIELDS YES -> (none); STATUS Released -> (none); Specifications (none) -> 1.5k, 1%, 1/16W, 0402
- R267, R286: value ~ -> 0Ω_0402; footprint R0402 -> 4ms_Resistor:R_0402; symbol MCD_PARTS_database:U_STM32MP25XXAK Power_0_Resistor_MCD_PARTS_database.DbLib -> 4ms_Resistor_0402:0Ω_0402; ALTERNATE_MANUFACTURER N/A -> (none); ALTERNATE_MANUFACTURER_PART_NUMBER N/A -> (none); ALTIUM_VALUE 0R -> (none); COMPONENTLINK1DESCRIPTION Datasheet -> (none); COMPONENTLINK1URL http://tunmcdsvn.tun.st.com/Component_Documentation_Library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 -> (none); COMPONENT_COUNTRY_OF_ORIGIN China -> (none); Display (none) -> 0Ω; ECCN_EU NEC -> (none); ECCN_US EAR99 -> (none); ID 2540 -> (none); INITIAL_BOARD_REFERENCE mb1274 -> (none); INTERNAL_PART_NUMBER MCD-00052 -> (none); JLCPCB ID (none) -> C106231; MANUFACTURER YAGEO -> (none); MANUFACTURER_PART_NUMBER RC0402JR-070RL -> (none); Manufacturer (none) -> Yageo; ORDER_CODE_DIGIKEY 311-0.0JRCT-ND -> (none); ORDER_CODE_FARNELL 9232516RL -> (none); ORDER_CODE_RS 618-5804 -> (none); PACKAGE 0402 -> (none); PART_PREFERENCE Recommended -> (none); PART_TYPE Resistor -> (none); PROVIDED_BY SUBCO -> (none); Part Number (none) -> RC0402FR-070RL; Production Stage (none) -> A; SHOWFIELDS YES -> (none); STATUS Released -> (none); Specifications (none) -> 0Ω, 1%, 1/16W, 0402
- R57: value ~ -> 0Ω_0402; footprint R0402 -> 4ms_Resistor:R_0402; symbol MCD_PARTS_database:U_PMIC_1_Resistor_MCD_PARTS_database.DbLib -> 4ms_Resistor_0402:0Ω_0402; ALTERNATE_MANUFACTURER N/A -> (none); ALTERNATE_MANUFACTURER_PART_NUMBER N/A -> (none); ALTIUM_VALUE 0R -> (none); COMPONENTLINK1DESCRIPTION Datasheet -> (none); COMPONENTLINK1URL http://tunmcdsvn.tun.st.com/Component_Documentation_Library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 -> (none); COMPONENT_COUNTRY_OF_ORIGIN China -> (none); Display (none) -> 0Ω; ECCN_EU NEC -> (none); ECCN_US EAR99 -> (none); ID 2540 -> (none); INITIAL_BOARD_REFERENCE mb1274 -> (none); INTERNAL_PART_NUMBER MCD-00052 -> (none); JLCPCB ID (none) -> C106231; MANUFACTURER YAGEO -> (none); MANUFACTURER_PART_NUMBER RC0402JR-070RL -> (none); Manufacturer (none) -> Yageo; ORDER_CODE_DIGIKEY 311-0.0JRCT-ND -> (none); ORDER_CODE_FARNELL 9232516RL -> (none); ORDER_CODE_RS 618-5804 -> (none); PACKAGE 0402 -> (none); PART_PREFERENCE Recommended -> (none); PART_TYPE Resistor -> (none); PROVIDED_BY SUBCO -> (none); Part Number (none) -> RC0402FR-070RL; Production Stage (none) -> A; SHOWFIELDS YES -> (none); STATUS Released -> (none); Specifications (none) -> 0Ω, 1%, 1/16W, 0402
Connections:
- net +1V8: now also C152.1, C157.1, C193.1, C220.1, C236.1, C237.1, C238.1, C239.1, C240.1, C246.1, C253.1; no longer C152.2, C157.2, C193.2, C220.2, C236.2, C237.2, C238.2, C239.2, C240.2, C246.2, C253.2
- net +3V3: now also C154.1, C204.1, C206.1, C207.1, C21.1; no longer C154.2, C204.2, C206.2, C207.2, C21.2
- net +5V: now also C153.1, C184.1, C188.1, C199.1, C20.1, C209.1, C29.1, C30.1, C32.1, C38.1; no longer C153.2, C184.2, C188.2, C199.2, C20.2, C209.2, C29.2, C30.2, C32.2, C38.2
- net GND: now also C1.2, C10.2, C11.2, C13.2, C15.2, C152.2, C153.2, C154.2, C156.2, C157.2, C16.2, C17.2, C183.2, C184.2, C186.2, C187.2, C188.2, C189.2, C19.2, C192.2, C193.2, C195.2, C196.2, C199.2, C2.2, C20.2, C200.2, C201.2, C202.2, C204.2, C206.2, C207.2, C209.2, C21.2, C22.2, C220.2, C225.2, C23.2, C234.2, C235.2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; no longer C1.1, C10.1, C11.1, C13.1, C15.1, C152.1, C153.1, C154.1, C156.1, C157.1, C16.1, C17.1, C183.1, C184.1, C186.1, C187.1, C188.1, C189.1, C19.1, C192.1, C193.1, C195.1, C196.1, C199.1, C2.1, C20.1, C200.1, C201.1, C202.1, C204.1, C206.1, C207.1, C209.1, C21.1, C22.1, C220.1, C225.1, C23.1, C234.1, C235.1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
- net NRST: now also C33.1; no longer C33.2
- net VDDA_1V8: now also C189.1, C234.1; no longer C189.2, C234.2
- net VDDIO_SDCARD: now also C195.1; no longer C195.2
- net VDD_CORE: now also C16.1, C183.1, C192.1, C201.1, C22.1, C23.1, C24.1, C45.1, C46.1, C48.1, C49.1, C50.1, C51.1; no longer C16.2, C183.2, C192.2, C201.2, C22.2, C23.2, C24.2, C45.2, C46.2, C48.2, C49.2, C50.2, C51.2
- net VDD_CPU: now also C10.1, C11.1, C26.1, C27.1, C28.1, C64.1, C68.1, C69.1, C7.1; no longer C10.2, C11.2, C26.2, C27.2, C28.2, C64.2, C68.2, C69.2, C7.2
- net VDD_DDR: now also C13.1, C200.1, C202.1, C39.1, C41.1, C75.1, C76.1, C82.1; no longer C13.2, C200.2, C202.2, C39.2, C41.2, C75.2, C76.2, C82.2
- net VDD_GPU: now also C1.1, C2.1, C3.1, C34.1, C35.1, C36.1, C37.1, C4.1, C5.1, C52.1, C58.1, C59.1; no longer C1.2, C2.2, C3.2, C34.2, C35.2, C36.2, C37.2, C4.2, C5.2, C52.2, C58.2, C59.2
- net VDD_IO: now also C17.1, C186.1, C187.1, C19.1, C196.1, C71.1, C72.1, C74.1, C87.1; no longer C17.2, C186.2, C187.2, C19.2, C196.2, C71.2, C72.2, C74.2, C87.2
- net VDD_USB: now also C156.1; no longer C156.2
- net VREF+: now also C248.1; no longer C248.2
- net VTT_DDR: now also C40.1; no longer C40.2
- net at R267.1, U1.AB6 (VDDA18ADC): now also C235.1, C244.1; no longer C235.2, C244.2
- net at R286.2, U1.AE21 (VDD33USB), U1.AE22 (VDD33UCPD): now also C251.1; no longer C251.2
- net at U1.R7 (V08CAP): now also C225.1; no longer C225.2
- net at R11.2, U1.AB20 (VDDCOMBOPHY), U1.AB22 (VDDCOMBOPHYTX)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: now also C15.1, C252.1, C260.1; no longer C15.2, C252.2, C260.2
- net at U26.12 (VBUS): now also R57.1; no longer R57.2
- net at U26.45 (REFDDR): now also C43.1; no longer C43.2
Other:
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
